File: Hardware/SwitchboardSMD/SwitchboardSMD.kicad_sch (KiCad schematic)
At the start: 46 parts, among them J2 S88_In_Plug, J4 S88_Out_Plug, Q1 MMBT5551L, SW1 SW_Push, SW2 SW_Push, SW3 SW_Push, SW4 SW_Push, SW5 SW_Push, SW6 SW_Push, SW7 SW_Push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

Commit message: Updated Geometry
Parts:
- J2: value S88_In_Plug -> S88_In
- J4: value S88_Out_Plug -> S88_Out
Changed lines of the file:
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@@
 			)
 		)
-		(property "Value" "S88_In_Plug"
+		(property "Value" "S88_In"
 			(at 262.382 101.5746 0)
 			(effects
@@
 			)
 		)
-		(property "Value" "S88_Out_Plug"
+		(property "Value" "S88_Out"
 			(at 262.382 137.1346 0)
 			(effects

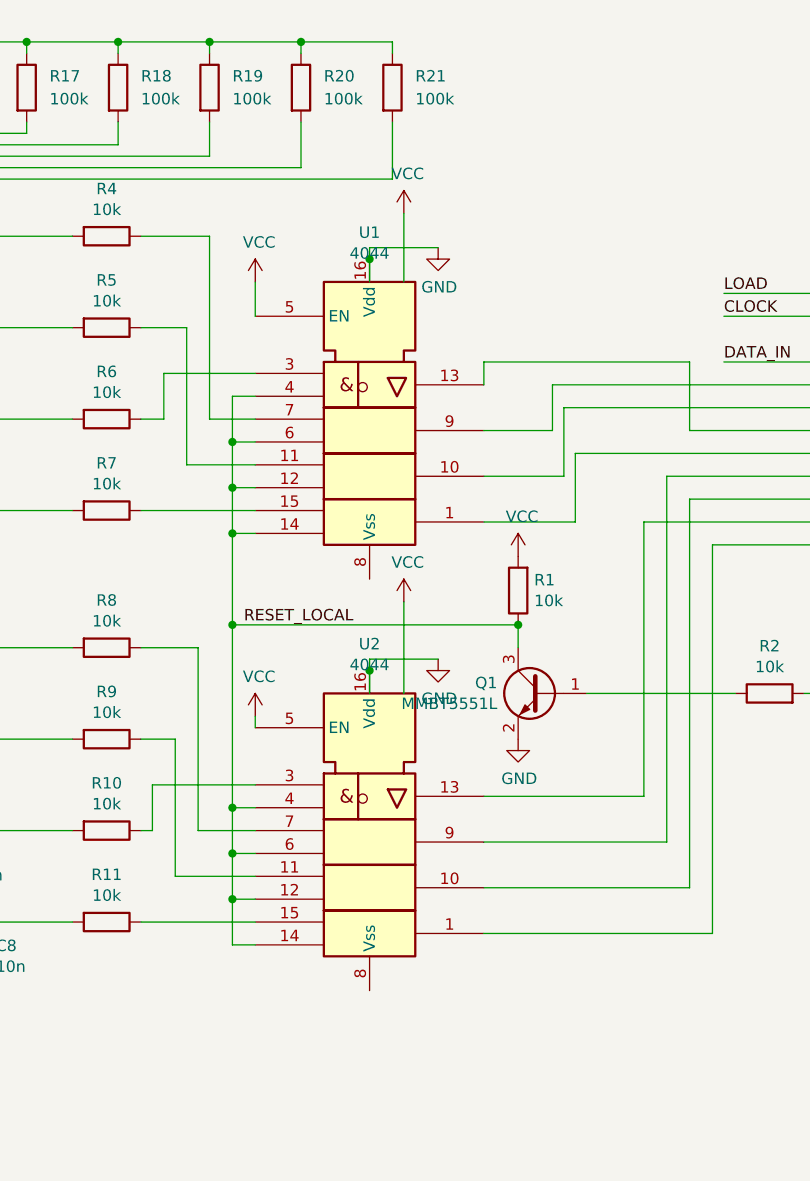
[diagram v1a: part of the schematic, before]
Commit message: Fix VCC/GND assignment
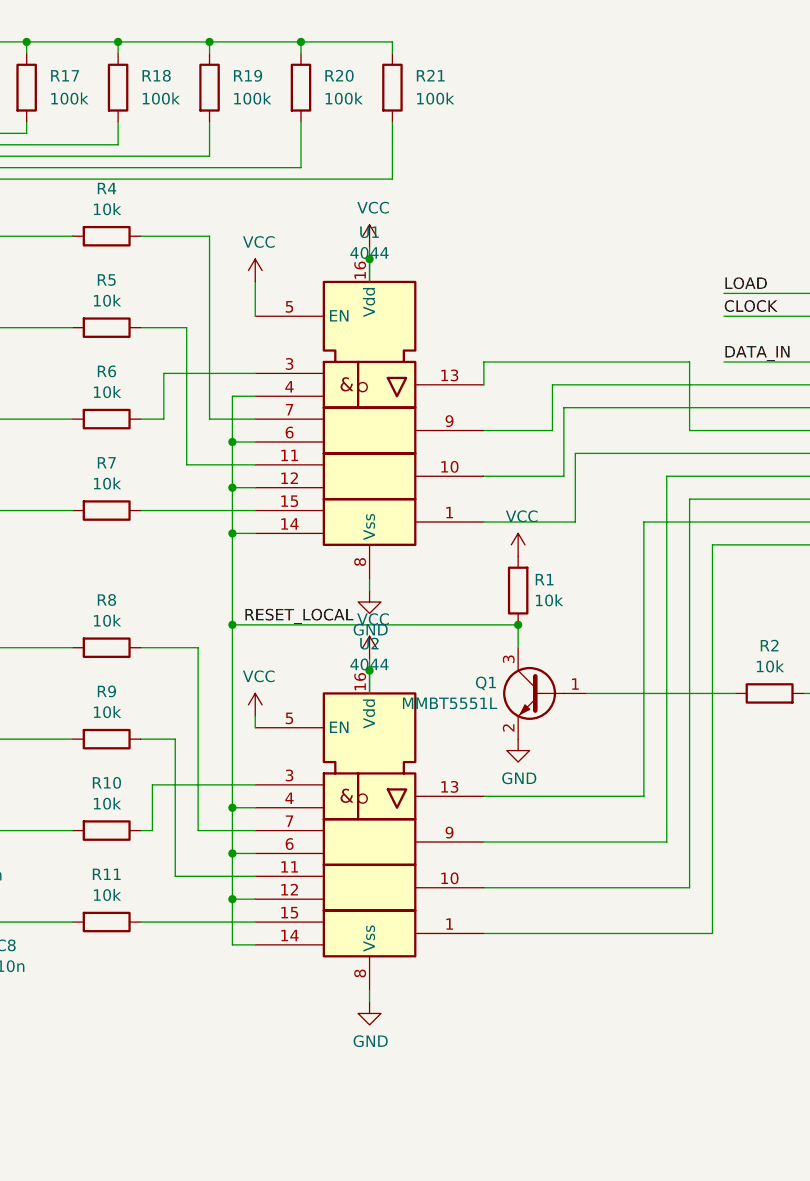
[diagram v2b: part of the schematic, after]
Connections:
- net GND: now also U1.8 (Vss), U2.8 (Vss); no longer U1.16 (Vdd), U2.16 (Vdd)
- net VCC: now also U1.16 (Vdd), U2.16 (Vdd)
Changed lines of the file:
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@@
 	(wire
 		(pts
-			(xy 133.35 91.44) (xy 133.35 81.28)
-		)
-		(stroke
-			(width 0)
-			(type default)
-		)
-	)
-	(wire
-		(pts
 			(xy 67.31 93.98) (xy 67.31 104.14)
 		)
@@
 	(wire
 		(pts
-			(xy 137.16 41.91) (xy 129.54 41.91)
-		)
-		(stroke
-			(width 0)
-			(type default)
-		)
-	)
-	(wire
-		(pts
-			(xy 129.54 87.63) (xy 137.16 87.63)
-		)
-		(stroke
-			(width 0)
-			(type default)
-		)
-	)
-	(wire
-		(pts
 			(xy 104.14 86.36) (xy 110.49 86.36)
 		)
@@
 	(wire
 		(pts
-			(xy 133.35 45.72) (xy 133.35 38.1)
-		)
-		(stroke
-			(width 0)
-			(type default)
-		)
-	)
-	(wire
-		(pts
 			(xy 165.1 62.23) (xy 179.07 62.23)
 		)
@@
 	(wire
 		(pts
+			(xy 129.54 124.46) (xy 129.54 125.73)
+		)
+		(stroke
+			(width 0)
+			(type default)
+		)
+	)
+	(wire
+		(pts
 			(xy 241.3 49.53) (xy 241.3 41.91)
 		)
@@
 	(wire
 		(pts
+			(xy 129.54 78.74) (xy 129.54 80.01)
+		)
+		(stroke
+			(width 0)
+			(type default)
+		)
+	)
+	(wire
+		(pts
 			(xy 107.95 111.76) (xy 116.84 111.76)
 		)
@@
 	(symbol
 		(lib_id "power:GND")
-		(at 137.16 87.63 0)
+		(at 129.54 125.73 0)
 		(unit 1)
 		(exclude_from_sim no)
@@
 		(dnp no)
 		(property "Reference" "#PWR0101"
-			(at 137.16 93.98 0)
+			(at 129.54 132.08 0)
 			(effects
 				(font
@@
 		)
 		(property "Value" "GND"
-			(at 137.287 92.0242 0)
+			(at 129.667 130.1242 0)
 			(effects
 				(font
@@
 		)
 		(property "Footprint" ""
-			(at 137.16 87.63 0)
+			(at 129.54 125.73 0)
 			(effects
 				(font
@@
 		)
 		(property "Datasheet" ""
-			(at 137.16 87.63 0)
+			(at 129.54 125.73 0)
 			(effects
 				(font
@@
 		)
 		(property "Description" ""
-			(at 137.16 87.63 0)
+			(at 129.54 125.73 0)
 			(effects
 				(font
@@
 	(symbol
 		(lib_id "power:GND")
-		(at 137.16 41.91 0)
+		(at 129.54 80.01 0)
 		(unit 1)
 		(exclude_from_sim no)
@@
 		(dnp no)
 		(property "Reference" "#PWR0102"
-			(at 137.16 48.26 0)
+			(at 129.54 86.36 0)
 			(effects
 				(font
@@
 		)
 		(property "Value" "GND"
-			(at 137.287 46.3042 0)
+			(at 129.667 84.4042 0)
 			(effects
 				(font
@@
 		)
 		(property "Footprint" ""
-			(at 137.16 41.91 0)
+			(at 129.54 80.01 0)
 			(effects
 				(font
@@
 		)
 		(property "Datasheet" ""
-			(at 137.16 41.91 0)
+			(at 129.54 80.01 0)
 			(effects
 				(font
@@
 		)
 		(property "Description" ""
-			(at 137.16 41.91 0)
+			(at 129.54 80.01 0)
 			(effects
 				(font
@@
 	(symbol
 		(lib_id "power:VCC")
-		(at 133.35 81.28 0)
+		(at 129.54 87.63 0)
 		(unit 1)
 		(exclude_from_sim no)
@@
 		(dnp no)
 		(property "Reference" "#PWR0103"
-			(at 133.35 85.09 0)
+			(at 129.54 91.44 0)
 			(effects
 				(font
@@
 		)
 		(property "Value" "VCC"
-			(at 133.7818 76.8858 0)
+			(at 129.9718 83.2358 0)
 			(effects
 				(font
@@
 		)
 		(property "Footprint" ""
-			(at 133.35 81.28 0)
+			(at 129.54 87.63 0)
 			(effects
 				(font
@@
 		)
 		(property "Datasheet" ""
-			(at 133.35 81.28 0)
+			(at 129.54 87.63 0)
 			(effects
 				(font
@@
 		)
 		(property "Description" ""
-			(at 133.35 81.28 0)
+			(at 129.54 87.63 0)
 			(effects
 				(font
@@
 	(symbol
 		(lib_id "power:VCC")
-		(at 133.35 38.1 0)
+		(at 129.54 41.91 0)
 		(unit 1)
 		(exclude_from_sim no)
@@
 		(dnp no)
 		(property "Reference" "#PWR0104"
-			(at 133.35 41.91 0)
+			(at 129.54 45.72 0)
 			(effects
 				(font
@@
 		)
 		(property "Value" "VCC"
-			(at 133.7818 33.7058 0)
+			(at 129.9718 37.5158 0)
 			(effects
 				(font
@@
 		)
 		(property "Footprint" ""
-			(at 133.35 38.1 0)
+			(at 129.54 41.91 0)
 			(effects
 				(font
@@
 		)
 		(property "Datasheet" ""
-			(at 133.35 38.1 0)
+			(at 129.54 41.91 0)
 			(effects
 				(font
@@
 		)
 		(property "Description" ""
-			(at 133.35 38.1 0)
+			(at 129.54 41.91 0)
 			(effects
 				(font

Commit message: Updated production files
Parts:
- H1, H2, H3, H4: footprint MountingHole:MountingHole_2.2mm_M2_Pad_Via -> MountingHole:MountingHole_2.2mm_M2
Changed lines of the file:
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@@
 			)
 		)
-		(property "Footprint" "MountingHole:MountingHole_2.2mm_M2_Pad_Via"
+		(property "Footprint" "MountingHole:MountingHole_2.2mm_M2"
 			(at 246.38 39.37 0)
 			(effects
@@
 			)
 		)
-		(property "Footprint" "MountingHole:MountingHole_2.2mm_M2_Pad_Via"
+		(property "Footprint" "MountingHole:MountingHole_2.2mm_M2"
 			(at 246.38 46.99 0)
 			(effects
@@
 			)
 		)
-		(property "Footprint" "MountingHole:MountingHole_2.2mm_M2_Pad_Via"
+		(property "Footprint" "MountingHole:MountingHole_2.2mm_M2"
 			(at 246.38 54.61 0)
 			(effects
@@
 			)
 		)
-		(property "Footprint" "MountingHole:MountingHole_2.2mm_M2_Pad_Via"
+		(property "Footprint" "MountingHole:MountingHole_2.2mm_M2"
 			(at 246.38 62.23 0)
 			(effects

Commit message: Files as sent for production
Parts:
- added H5: MountingHole_Pad, MountingHole:MountingHole_3.2mm_M3_Pad_Via, symbol Mechanical:MountingHole_Pad
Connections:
- net GND: now also H5.1
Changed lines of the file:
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@@
 	)
 	(junction
+		(at 241.3 41.91)
+		(diameter 0)
+		(color 0 0 0 0)
+	)
+	(junction
 		(at 67.31 114.3)
 		(diameter 0)
@@
 	(wire
 		(pts
+			(xy 219.71 41.91) (xy 241.3 41.91)
+		)
+		(stroke
+			(width 0)
+			(type default)
+		)
+	)
+	(wire
+		(pts
 			(xy 255.27 81.28) (xy 245.11 81.28)
 		)
@@
 					(unit 1)
 				)
+			)
+		)
+	)
+	(symbol
+		(lib_id "Mechanical:MountingHole_Pad")
+		(at 219.71 39.37 0)
+		(unit 1)
+		(exclude_from_sim no)
+		(in_bom yes)
+		(on_board yes)
+		(dnp no)
+		(property "Reference" "H5"
+			(at 222.25 38.1254 0)
+			(effects
+				(font
+					(size 1.27 1.27)
+				)
+				(justify left)
+			)
+		)
+		(property "Value" "MountingHole_Pad"
+			(at 222.25 40.4368 0)
+			(effects
+				(font
+					(size 1.27 1.27)
+				)
+				(justify left)
+			)
+		)
+		(property "Footprint" "MountingHole:MountingHole_3.2mm_M3_Pad_Via"
+			(at 219.71 39.37 0)
+			(effects
+				(font
+					(size 1.27 1.27)
+				)
+				(hide yes)
+			)
+		)
+		(property "Datasheet" "~"
+			(at 219.71 39.37 0)
+			(effects
+				(font
+					(size 1.27 1.27)
+				)
+				(hide yes)
+			)
+		)
+		(property "Description" ""
+			(at 219.71 39.37 0)
+			(effects
+				(font
+					(size 1.27 1.27)
+				)
+			)
+		)
+		(pin "1"
+		)
+		(instances
+			(project "SwitchboardSMD"
+				(path "/ac4976cf-0d78-436d-a3bb-0ec53681a8b4"
+					(reference "H5")
+					(unit 1)
+				)
